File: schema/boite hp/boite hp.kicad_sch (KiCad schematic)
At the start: 0 parts

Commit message: Design bracelet PCB
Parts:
- added C1, C2: 1u, Capacitor_SMD:C_0805_2012Metric, symbol Device:C
- added F1: Polyfuse, symbol Device:Polyfuse
- added J1: IN-, symbol Connector:Conn_01x01_Socket
- added J2: IN+, symbol Connector:Conn_01x01_Socket
- added J3: B+, symbol Connector:Conn_01x01_Socket
- added J4: B-, symbol Connector:Conn_01x01_Socket
- added J5: Bracelet+, symbol Connector:Conn_01x01_Pin
- added J6: Bracelet-, symbol Connector:Conn_01x01_Pin
- added J7: HP+, symbol Connector:Conn_01x01_Socket
- added J8: HP-, symbol Connector:Conn_01x01_Socket
- added R1, R2: 100K, symbol Device:R
- added R3, R4: 1k, symbol Device:R
- added R5: 10k, symbol Device:R
- added U1, U2: (no value), Library_Perso:IP2312, symbol Library_Perso:IP2312-charger
- added U3: (no value), Library_Perso:ESP-32D devkit, symbol Library_Perso:ESP-32D_Devkit
- added U4: LDO 3v3, Package_TO_SOT_SMD:SOT-223-3_TabPin2, symbol Power_Management:AUIPS1051L
- added U5: (no value), Library_Perso:PCM5102A Module, symbol Library_Perso:PCM5102A_Module
- added U6: (no value), Library_Perso:PAM8403 Module, symbol Library_Perso:PAM8403_Module
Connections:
- new net: C2.1, J3.1 (Pin_1), R1.1, U1.B+, U4.3 (S)
- new net: F1.1, J5.1 (Pin_1)
- new net: J7.1 (Pin_1), U6.L+
- new net: R1.2, R2.2, U3.34 (IO34)
- new net: U3.25 (IO25), U5.BCK
- new net: R5.1, U3.26 (IO26), U5.XSMT
- new net: U3.32 (IO32), U5.LRCK
- new net: U3.33 (IO33), U5.DIN
- new net: U5.AGND, U6.G
- new net: R4.1, U5.LOUT
- new net: R3.1, U5.ROUT
- new net: J2.1 (Pin_1), U1.IN+, U2.IN+
- new net: J8.1 (Pin_1), U6.L-
- new net: R3.2, R4.2, U6.L
- new net: F1.2, U2.B+
- new net +3.3V: C1.1, R5.2, U3.3V3, U4.2 (D), U5.VIN, U6.+
- new net GND: C1.2, C2.2, J1.1 (Pin_1), J4.1 (Pin_1), J6.1 (Pin_1), R2.1, U1.B-, U1.IN-, U2.B-, U2.IN-, U3.GND, U4.1 (IN), U5.GND, U6.GND
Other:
- note added: "100NF CERAMIQUE ET 470-1000UF ELECTROLYTIIQUE POUR PAM8403"
- note added: "100NF CERAMIQUE POUR PCM5102A"

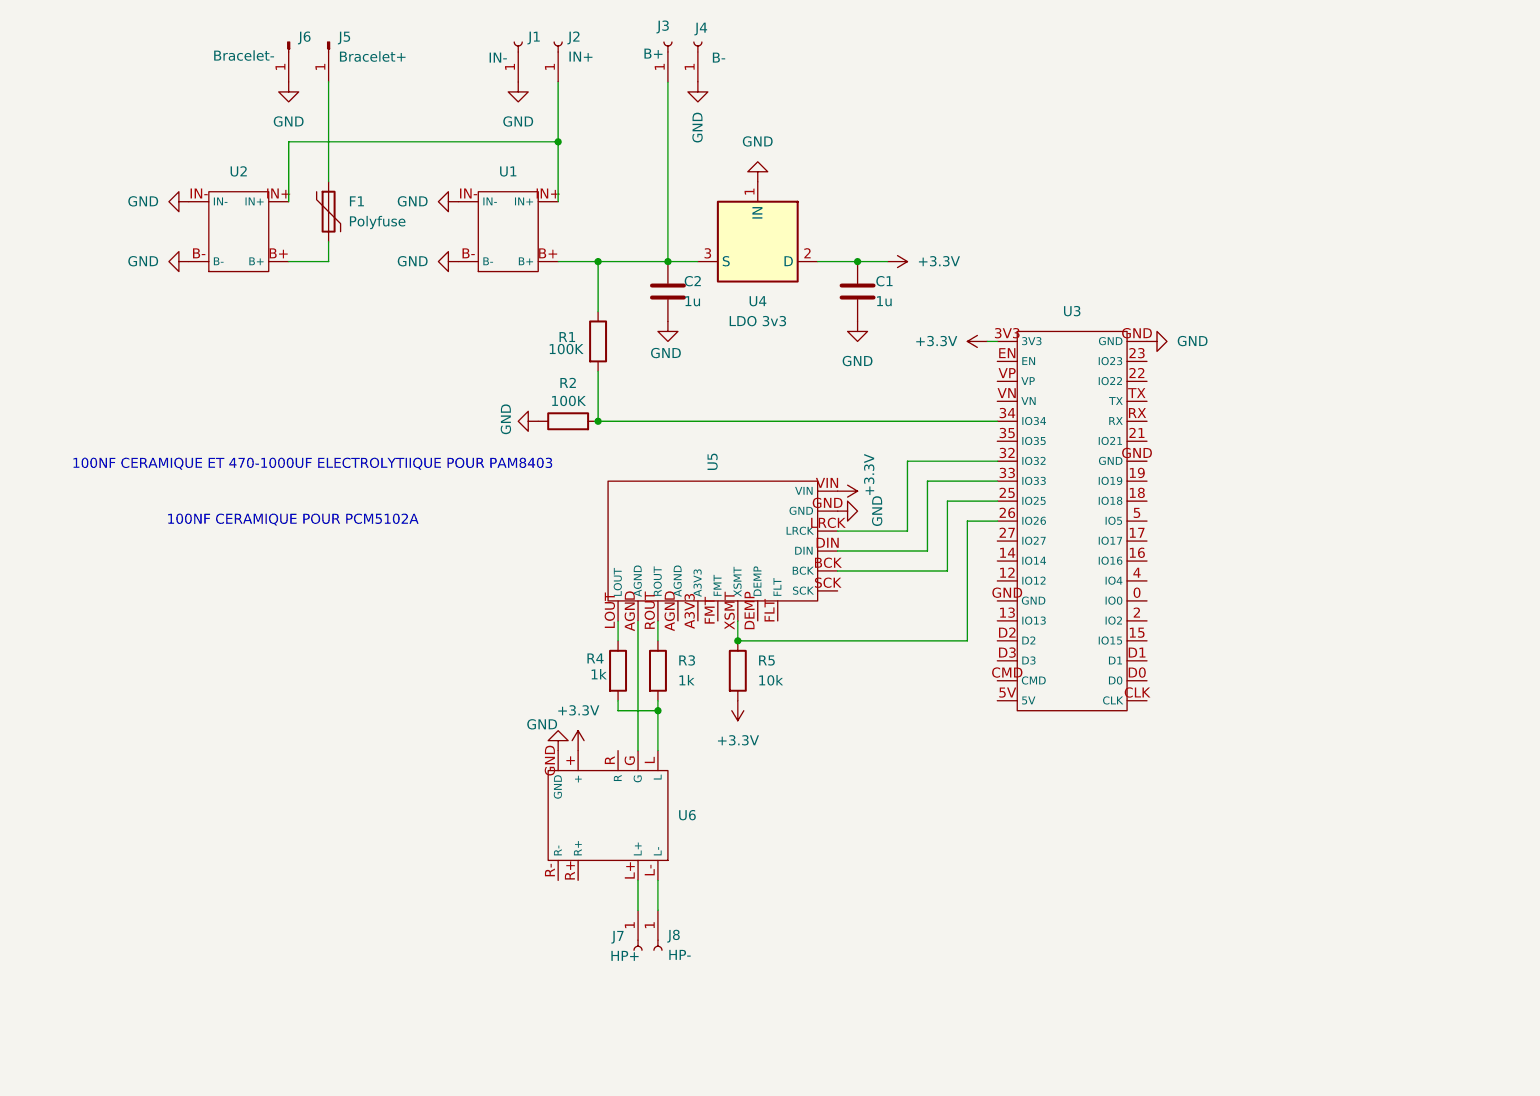
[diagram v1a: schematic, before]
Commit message: Add boite hp schema
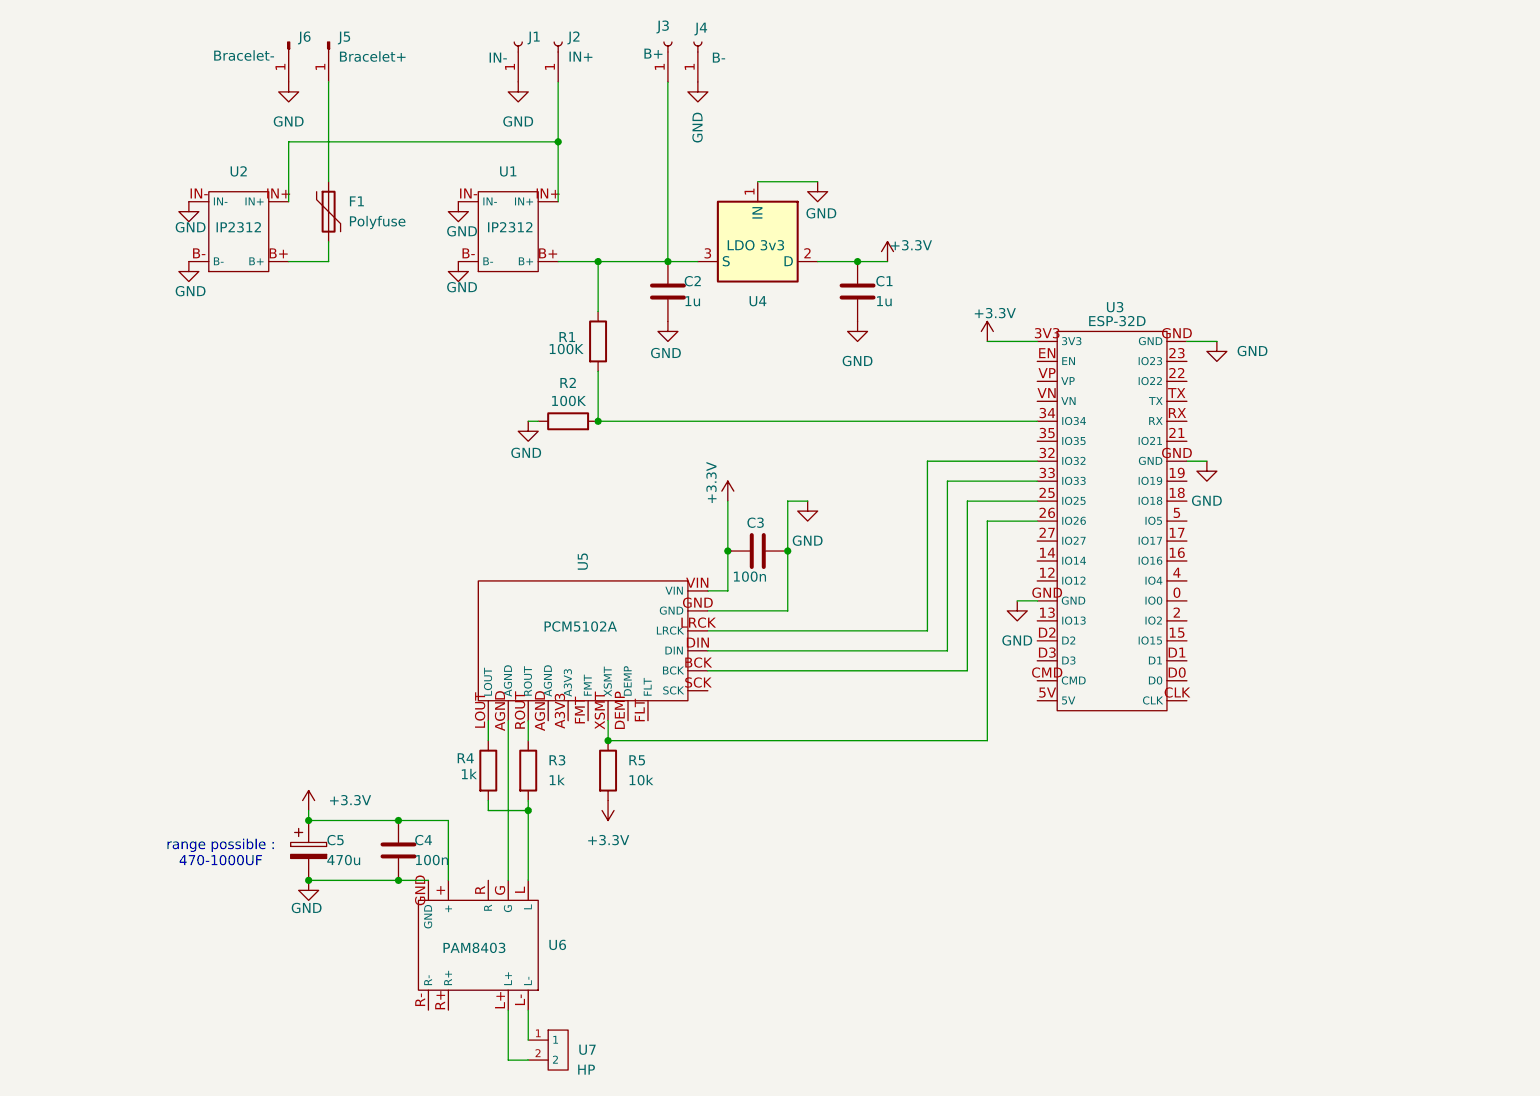
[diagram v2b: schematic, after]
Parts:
- removed J7: HP+, symbol Connector:Conn_01x01_Socket
- removed J8: HP-, symbol Connector:Conn_01x01_Socket
- added C3, C4: 100n, Capacitor_SMD:C_0805_2012Metric, symbol Device:C
- added C5: 470u, Capacitor_THT:CP_Radial_D8.0mm_P3.50mm, symbol Device:C_Polarized
- added U7: HP, Library_Perso:Connector_boxed_2.54_1x02, symbol Library_Perso:connector_boxed_2.54mm_1x02
- F1: footprint (none) -> Capacitor_THT:C_Disc_D5.0mm_W2.5mm_P5.00mm
- J1, J2, J3, J4, J5, J6: footprint (none) -> Connector_Wire:SolderWirePad_1x01_SMD_2x4mm
- R1, R2, R3, R4, R5: footprint (none) -> Resistor_SMD:R_1206_3216Metric
- U1, U2: value (none) -> IP2312
- U3: value (none) -> ESP-32D
- U5: value (none) -> PCM5102A
- U6: value (none) -> PAM8403
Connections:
- net +3.3V: now also C3.1, C4.1, C5.1
- net GND: now also C3.2, C4.2, C5.2
- net at U6.L+: now also U7.2
- net at U5.AGND: now also U6.G
- net at U6.L-: now also U7.1
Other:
- note added: "range possible : 470-1000UF"
- note removed: "100NF CERAMIQUE ET 470-1000UF ELECTROLYTIIQUE POUR PAM8403"
- note removed: "100NF CERAMIQUE POUR PCM5102A"
- moved on the sheet: R3, R4, R5, U3, U5, U6

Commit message: Update Architecture db
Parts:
- removed J1: IN-, Connector_Wire:SolderWirePad_1x01_SMD_2x4mm, symbol Connector:Conn_01x01_Socket
- removed J2: IN+, Connector_Wire:SolderWirePad_1x01_SMD_2x4mm, symbol Connector:Conn_01x01_Socket
- removed J3: B+, Connector_Wire:SolderWirePad_1x01_SMD_2x4mm, symbol Connector:Conn_01x01_Socket
- removed J4: B-, Connector_Wire:SolderWirePad_1x01_SMD_2x4mm, symbol Connector:Conn_01x01_Socket
- removed J5: Bracelet+, Connector_Wire:SolderWirePad_1x01_SMD_2x4mm, symbol Connector:Conn_01x01_Pin
- removed J6: Bracelet-, Connector_Wire:SolderWirePad_1x01_SMD_2x4mm, symbol Connector:Conn_01x01_Pin
- removed U7: HP, Library_Perso:Connector_boxed_2.54_1x02, symbol Library_Perso:connector_boxed_2.54mm_1x02
- added J1: IN, Connector_JST:JST_PH_B2B-PH-K_1x02_P2.00mm_Vertical, symbol Connector:Conn_01x02_Socket
- added J2: Bracelet, Connector_JST:JST_PH_B2B-PH-K_1x02_P2.00mm_Vertical, symbol Connector:Conn_01x02_Socket
- added J3: Battery, Connector_JST:JST_PH_B2B-PH-K_1x02_P2.00mm_Vertical, symbol Connector:Conn_01x02_Socket
- added J4: res1, Connector_JST:JST_PH_B2B-PH-K_1x02_P2.00mm_Vertical, symbol Connector:Conn_01x02_Socket
- added J5: res2, Connector_JST:JST_PH_B2B-PH-K_1x02_P2.00mm_Vertical, symbol Connector:Conn_01x02_Socket
- added J7: HP, Connector_JST:JST_PH_B2B-PH-K_1x02_P2.00mm_Vertical, symbol Connector:Conn_01x02_Socket
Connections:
- net GND: now also J1.1 (Pin_1), J2.1 (Pin_1), J3.1 (Pin_1), J4.1 (Pin_1), J5.1 (Pin_1)
- net at C2.1, R1.1, U1.B+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: now also J3.2 (Pin_2)
- net at U6.L-: now also J7.1 (Pin_1)
- net at U6.L+: now also J7.2 (Pin_2)
- net at F1.1: now also J2.2 (Pin_2)
- net at U3.22 (IO22): now also J4.2 (Pin_2)
- net at U3.23 (IO23): now also J5.2 (Pin_2)
- net at U5.AGND: now also U6.G
- net at U1.IN+, U2.IN+: now also J1.2 (Pin_2)
